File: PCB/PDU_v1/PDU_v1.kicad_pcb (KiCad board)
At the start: 2 copper layers, 57.6 x 60.8 mm, 64 parts, among them J1 Conn_01x02_Pin, J10 Screw_Terminal_01x01, J11 Screw_Terminal_01x01, J12 Screw_Terminal_01x01, J13 Screw_Terminal_01x01, J14 Conn_01x04_Pin, J2 Screw_Terminal_01x01, J3 Screw_Terminal_01x01, J4 Screw_Terminal_01x01, J5 Screw_Terminal_01x01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

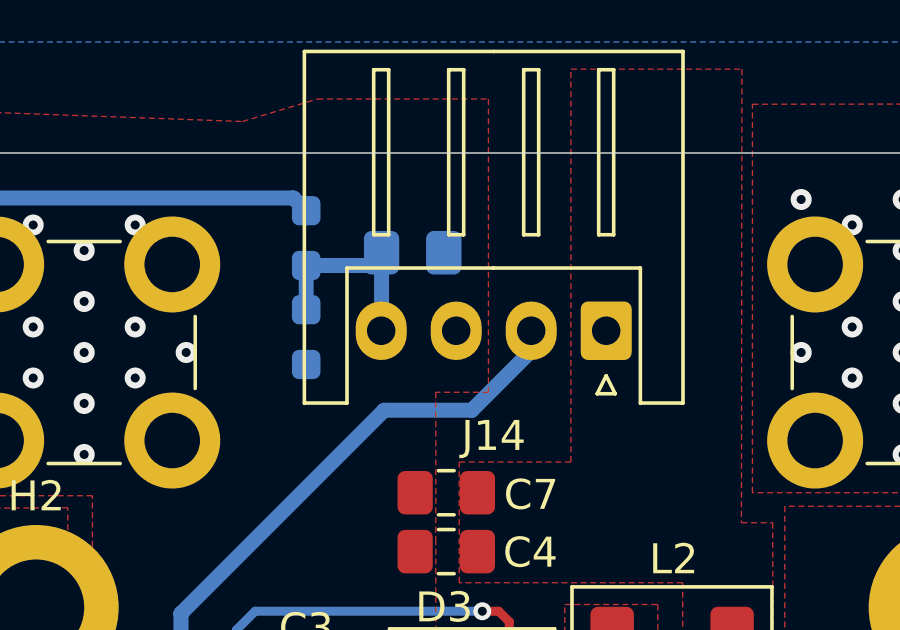
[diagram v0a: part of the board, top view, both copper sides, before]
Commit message: Update PCB nets, footprint positions and routes
Rename and reassign nets for clarity (e.g. Net-(J14-Pin_4) -> BAT_VOL, adjust BAT_CURR and /BAT_IN/GND assignments), adjust component placement (C30 moved and value normalized from "0.1uF" to "100n"), and update board routing (track segment coordinates and UUIDs, zone polygon points). Add a PCB backup archive (PDU_v1-2026-02-05_204958.zip). These changes align footprints, nets and routing; schematic was also updated to keep the design consistent.
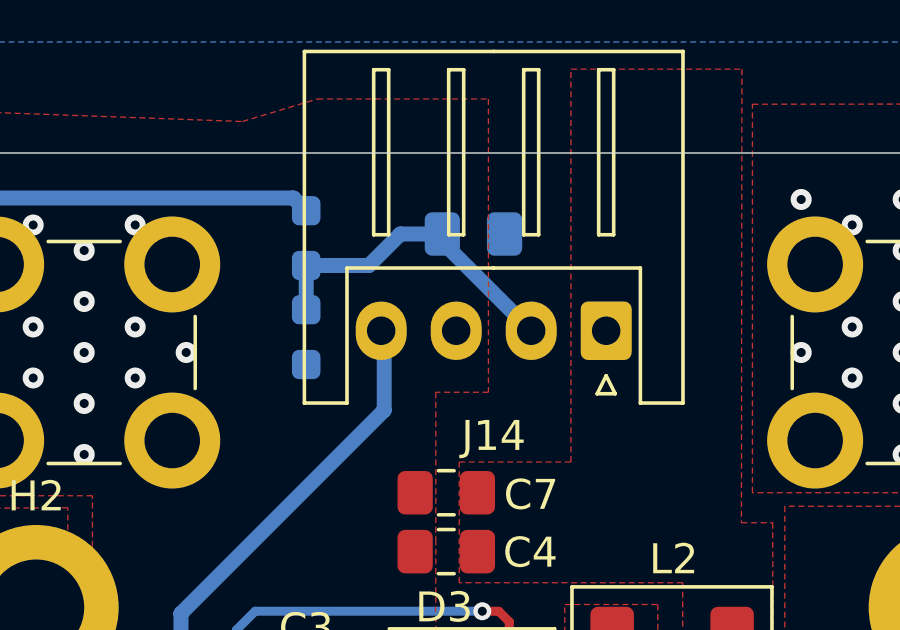
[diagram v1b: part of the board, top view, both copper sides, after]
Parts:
- C30: value 0.1uF -> 100n
- moved C30 2.12 mm to (156.6, 38.0)
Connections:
- C30 pad 2: Net-(J14-Pin_4) -> BAT_VOL
- J1 pad 1: GND -> /BAT_IN
- J1 pad 2: /BAT_IN -> GND
- J14 pad 2: BAT_CURR -> BAT_VOL
- J14 pad 4: Net-(J14-Pin_4) -> BAT_CURR
- R10 pad 2: Net-(J14-Pin_4) -> BAT_VOL
- R9 pad 1: Net-(J14-Pin_4) -> BAT_VOL
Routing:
- net BAT_VOL: track 0.00 -> 11.6 mm
- net Net-(J14-Pin_4): track 6.77 -> 0.00 mm
- net BAT_CURR: track 35.5 -> 31.8 mm
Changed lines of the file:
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@@
 	(net 17 "/SH_IN")
 	(net 18 "Net-(R8-Pad2)")
-	(net 19 "Net-(J14-Pin_4)")
+	(net 19 "BAT_VOL")
 	(footprint "Capacitor_SMD:C_0805_2012Metric_Pad1.18x1.45mm_HandSolder"
 		(layer "F.Cu")
@@
 			(remove_unused_layers no)
 			(roundrect_rratio 0.25)
-			(net 5 "GND")
+			(net 15 "/BAT_IN")
 			(pinfunction "Pin_1")
 			(pintype "passive")
@@
 			(layers "*.Cu" "*.Mask")
 			(remove_unused_layers no)
-			(net 15 "/BAT_IN")
+			(net 5 "GND")
 			(pinfunction "Pin_2")
 			(pintype "passive")
@@
 			(layers "*.Cu" "*.Mask")
 			(remove_unused_layers no)
-			(net 16 "BAT_CURR")
+			(net 19 "BAT_VOL")
 			(pinfunction "Pin_2")
 			(pintype "passive")
@@
 			(layers "*.Cu" "*.Mask")
 			(remove_unused_layers no)
-			(net 19 "Net-(J14-Pin_4)")
+			(net 16 "BAT_CURR")
 			(pinfunction "Pin_4")
 			(pintype "passive")
@@
 			(layers "B.Cu" "B.Mask" "B.Paste")
 			(roundrect_rratio 0.25)
-			(net 19 "Net-(J14-Pin_4)")
+			(net 19 "BAT_VOL")
 			(pintype "passive")
 		)
@@
 			(layers "B.Cu" "B.Mask" "B.Paste")
 			(roundrect_rratio 0.25)
-			(net 19 "Net-(J14-Pin_4)")
+			(net 19 "BAT_VOL")
 			(pintype "passive")
 		)
@@
 	(footprint "Capacitor_SMD:C_0805_2012Metric_Pad1.18x1.45mm_HandSolder"
 		(layer "B.Cu")
-		(at 154.55 38.675 180)
+		(at 156.575 38.05 180)
 		(descr "Capacitor SMD 0805 (2012 Metric), square (rectangular) end terminal, IPC-7351 nominal with elongated pad for handsoldering. (Body size source: IPC-SM-782 page 76, https://www.pcb-3d.com/wordpress/wp-content/uploads/ipc-sm-782a_amendment_1_and_2.pdf, https://docs.google.com/spreadsheets/d/1BsfQQcO9C6DZCsRaXUlFlo91Tg2WpOkGARC1WS5S8t0/edit?usp=sharing), generated with kicad-footprint-generator")
 		(tags "capacitor handsolder")
@@
 			)
 		)
-		(property "Value" "0.1uF"
+		(property "Value" "100n"
 			(at 0 -1.68 0)
 			(layer "B.Fab")
@@
 			(layers "B.Cu" "B.Mask" "B.Paste")
 			(roundrect_rratio 0.212766)
-			(net 19 "Net-(J14-Pin_4)")
+			(net 19 "BAT_VOL")
 			(pintype "passive")
 		)
@@
 	)
 	(segment
-		(start 153.6 43.925)
-		(end 156.525 43.925)
+		(start 149.3375 68.55)
+		(end 148.2 68.55)
 		(width 0.5)
 		(layer "B.Cu")
@@
 	)
 	(segment
-		(start 146.825 67.175)
-		(end 146.825 50.7)
+		(start 153.6 41.375)
+		(end 153.5 41.275)
 		(width 0.5)
 		(layer "B.Cu")
@@
 	)
 	(segment
-		(start 149.3375 68.55)
-		(end 148.2 68.55)
+		(start 153.5125 41.2625)
+		(end 153.5 41.275)
 		(width 0.5)
 		(layer "B.Cu")
@@
 	)
 	(segment
-		(start 148.2 68.55)
-		(end 146.825 67.175)
+		(start 146.825 67.175)
+		(end 146.825 50.7)
 		(width 0.5)
 		(layer "B.Cu")
@@
 	)
 	(segment
-		(start 146.825 50.7)
-		(end 153.6 43.925)
+		(start 148.2 68.55)
+		(end 146.825 67.175)
 		(width 0.5)
 		(layer "B.Cu")
@@
 	)
 	(segment
-		(start 156.525 43.925)
-		(end 158.5 41.95)
+		(start 146.825 50.7)
+		(end 153.6 43.925)
 		(width 0.5)
 		(layer "B.Cu")
@@
 	)
 	(segment
-		(start 158.5 41.95)
-		(end 158.5 41.275)
+		(start 153.6 43.925)
+		(end 153.6 41.375)
 		(width 0.5)
 		(layer "B.Cu")
@@
 	)
 	(segment
-		(start 151 39.1)
-		(end 153.0875 39.1)
+		(start 155.5375 38.05)
+		(end 155.5375 38.3125)
 		(width 0.5)
 		(layer "B.Cu")
@@
 	(segment
 		(start 153.0875 39.1)
-		(end 153.5125 38.675)
+		(end 154.1375 38.05)
 		(width 0.5)
 		(layer "B.Cu")
@@
 	)
 	(segment
-		(start 153.5125 41.2625)
-		(end 153.5 41.275)
+		(start 154.1375 38.05)
+		(end 155.5375 38.05)
+		(width 0.5)
+		(layer "B.Cu")
+		(net 19)
+	)
+	(segment
+		(start 155.5375 38.3125)
+		(end 158.5 41.275)
 		(width 0.5)
 		(layer "B.Cu")
@@
 	)
 	(segment
-		(start 153.5125 38.675)
-		(end 153.5125 41.2625)
+		(start 158.5 41.95)
+		(end 158.5 41.275)
+		(width 0.5)
+		(layer "B.Cu")
+		(net 19)
+	)
+	(segment
+		(start 151 39.1)
+		(end 153.0875 39.1)
 		(width 0.5)
 		(layer "B.Cu")
